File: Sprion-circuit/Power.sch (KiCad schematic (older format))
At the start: 27 parts, among them IC1 R3111N211A, IC2 TAR5SB50, J1 Conn_01x02_Female, Q1 Q_PMOS_GSD, Q2 Q_PMOS_GSD, SW1 SW_SPDT, U4 LXDC55FAAA-203

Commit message: Push, Push, Push
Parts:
- removed Q2: Q_PMOS_GSD, symbol Device:Q_PMOS_GSD
- added Q2: Q_NMOS_GSD, symbol Device:Q_NMOS_GSD
- C11: value C -> 0.1u
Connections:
- net +BATT: now also Q2.2 (S)
- net at C8.1, Q1.3 (D), R11.2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: now also Q2.3 (D)
- net at IC1.1 (OUT), R11.1: now also Q2.1 (G)
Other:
- moved on the sheet: C10, C11, C12, C13, C7, C8, C9, D1, IC1, IC2, J1, L1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

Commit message: :fix　いろいろ
後で書きます
とりあえず寝ます
許してください
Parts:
- added R32: 2.7, symbol Device:R
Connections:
- net +3.3VA: now also D1.2 (A)
- net +3V3: now also R32.2; no longer D1.2 (A), L1.1
- new net: L1.1, R32.1
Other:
- moved on the sheet: C12, C13, D1, L1, R12, R13, R14, R15, R16, R17, U4

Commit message: add,feat,fix:すまんコミットわすれててぐちゃぐちゃや
配置始めた。
フットプリント割り当てた
回路図pdfで吐いた
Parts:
- removed J1: Conn_01x02_Female, symbol Connector:Conn_01x02_Female
- removed U4: LXDC55FAAA-203, LXDC55FAAA203, symbol Sprion-circuit:LXDC55FAAA-203
- added C15: 0.1u, Capacitor_SMD:C_0603_1608Metric, symbol Device:C
- added J1: Conn_01x03_Female, Connector_JST:JST_PH_B3B-PH-K_1x03_P2.00mm_Vertical, symbol Connector:Conn_01x03_Female
- added R24, R25: 10k, Resistor_SMD:R_0603_1608Metric, symbol Device:R
- added U9: LXDC55FAAA-203, Sprion-circuit:LXDC55FAAA203, symbol Sprion-circuit:LXDC55FAAA-203
- C10, C11, C12, C13, C8, C9: footprint (none) -> Capacitor_SMD:C_0603_1608Metric
- C7: value CP -> 100u; footprint (none) -> Sprion-circuit:CAPPRD250W50D630H600
- D1: footprint (none) -> LED_SMD:LED_0603_1608Metric
- IC1, IC2: footprint (none) -> Package_TO_SOT_SMD:SOT-23-5
- L1: footprint (none) -> Inductor_SMD:L_1210_3225Metric
- Q1: value Q_PMOS_GSD -> IRML6402; footprint (none) -> Package_TO_SOT_SMD:SOT-23
- Q2: value Q_NMOS_GSD -> IRFML8244; footprint (none) -> Package_TO_SOT_SMD:SOT-23
- R10, R11, R12, R13, R14, R15, R16, R32, R7, R8, R9: footprint (none) -> Resistor_SMD:R_0603_1608Metric
- R17: value R -> 330; footprint (none) -> Resistor_SMD:R_0603_1608Metric
- SW1: value SW_SPDT -> SSAJ120100; footprint (none) -> Sprion-circuit:s
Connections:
- net +3.3VA: now also R24.1; no longer D1.2 (A)
- net +3V3: now also D1.2 (A), U9.7 (VOUT_1), U9.8 (VOUT_2), U9.9 (VOUT_3)
- net +BATT: now also U9.1 (EN), U9.3 (VIN_1)
- net GND: now also C15.2, J1.1 (Pin_1), R25.2, U9.12 (GND_2), U9.13 (GND_3), U9.14 (GND_4), U9.6 (GND_1)
- net at R12.2: now also U9.11 (FB)
- net at C7.1, Q1.2 (S), R7.2: now also J1.3 (Pin_3)
- new net: U9.4 (VIN_2), U9.5 (VIN_3)
- new net VREF: C15.1, R24.2, R25.1
- no-connect marks 1 -> 2

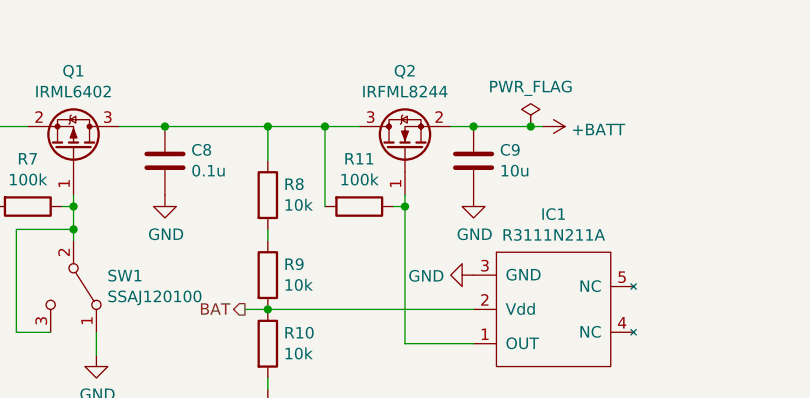
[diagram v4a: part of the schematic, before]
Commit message: fix: eschemaの微修正
ハイサイドスイッチをNch→Pchへ修正
bootをプルダウンに
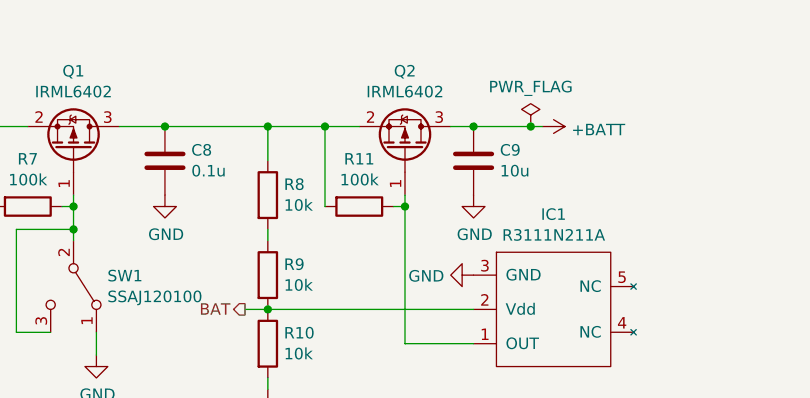
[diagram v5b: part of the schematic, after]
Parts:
- removed Q2: IRFML8244, Package_TO_SOT_SMD:SOT-23, symbol Device:Q_NMOS_GSD
- added Q2: IRML6402, Package_TO_SOT_SMD:SOT-23, symbol Device:Q_PMOS_GSD
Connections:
- net +BATT: now also Q2.3 (D)
- net at IC1.1 (OUT), R11.1: now also Q2.1 (G)
- net at C8.1, Q1.3 (D), R11.2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: now also Q2.2 (S)
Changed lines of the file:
@@
-$EndComp
-$Comp
-L Device:Q_NMOS_GSD Q2
-U 1 1 60E96580
-P 3950 2200
-F 0 "Q2" V 4292 2200 50  0000 C CNN
-F 1 "IRFML8244" V 4201 2200 50  0000 C CNN
-F 2 "Package_TO_SOT_SMD:SOT-23" H 4150 2300 50  0001 C CNN
-F 3 "~" H 3950 2200 50  0001 C CNN
-	1    3950 2200
-	0    -1   -1   0
 $EndComp
 $Comp
@@
 	0    -1   -1   0
 $EndComp
+$Comp
+L Device:Q_PMOS_GSD Q2
+U 1 1 61B67607
+P 3950 2200
+F 0 "Q2" V 4292 2200 50  0000 C CNN
+F 1 "IRML6402" V 4201 2200 50  0000 C CNN
+F 2 "Package_TO_SOT_SMD:SOT-23" H 4150 2300 50  0001 C CNN
+F 3 "~" H 3950 2200 50  0001 C CNN
+	1    3950 2200
+	0    1    -1   0
+$EndComp
 $EndSCHEMATC

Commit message: add fix feat: でけたー（コミットしてなくてごめん）
ベタ塗、配線、再配置等
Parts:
- removed Q2: IRML6402, Package_TO_SOT_SMD:SOT-23, symbol Device:Q_PMOS_GSD
- added Q2: IRFML8244, Package_TO_SOT_SMD:SOT-23, symbol Device:Q_NMOS_GSD
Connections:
- net +BATT: now also C8.1, Q1.3 (D), R8.1
- net GND: now also Q2.3 (D); no longer C7.2, C8.2, IC1.3 (GND), J1.1 (Pin_1), R10.2, SW1.1 (A)
- net at R11.1: now also C7.2, C8.2, IC1.3 (GND), J1.1 (Pin_1), R10.2, SW1.1 (A), Q2.2 (S); no longer IC1.1 (OUT)
- new net: IC1.1 (OUT), Q2.1 (G), R11.2
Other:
- moved on the sheet: C9, R11
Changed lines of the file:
@@
 $Descr A4 11693 8268
 encoding utf-8
-Sheet 2 6
+Sheet 6 6
 Title ""
 Date ""
@@
 $EndDescr
 $Comp
-L power:GND #PWR01
-U 1 1 60F3968F
-P 1400 2300
-F 0 "#PWR01" H 1400 2050 50  0001 C CNN
-F 1 "GND" V 1405 2172 50  0000 R CNN
-F 2 "" H 1400 2300 50  0001 C CNN
-F 3 "" H 1400 2300 50  0001 C CNN
-	1    1400 2300
-	0    -1   -1   0
-$EndComp
-$Comp
 L power:PWR_FLAG #FLG01
 U 1 1 60F3A851
-P 1350 2300
-F 0 "#FLG01" H 1350 2375 50  0001 C CNN
-F 1 "PWR_FLAG" H 1350 2473 50  0000 C CNN
-F 2 "" H 1350 2300 50  0001 C CNN
-F 3 "~" H 1350 2300 50  0001 C CNN
-	1    1350 2300
-	-1   0    0    1
-$EndComp
-Wire Wire Line
-	1300 2300 1350 2300
-Wire Wire Line
-	1350 2300 1400 2300
-Connection ~ 1350 2300
+P 1700 4650
+F 0 "#FLG01" H 1700 4725 50  0001 C CNN
+F 1 "PWR_FLAG" H 1700 4823 50  0000 C CNN
+F 2 "" H 1700 4650 50  0001 C CNN
+F 3 "~" H 1700 4650 50  0001 C CNN
+	1    1700 4650
+	0    -1   -1   0
+$EndComp
 $Comp
 L Switch:SW_SPDT SW1
@@
 $EndComp
 $Comp
-L power:GND #PWR03
-U 1 1 60F431E5
-P 2600 3100
-F 0 "#PWR03" H 2600 2850 50  0001 C CNN
-F 1 "GND" H 2605 2927 50  0000 C CNN
-F 2 "" H 2600 3100 50  0001 C CNN
-F 3 "" H 2600 3100 50  0001 C CNN
-	1    2600 3100
-	1    0    0    -1
-$EndComp
-$Comp
 L Device:R R7
 U 1 1 60F43B12
@@
 L power:+BATT #PWR08
 U 1 1 60F46202
-P 4550 2100
-F 0 "#PWR08" H 4550 1950 50  0001 C CNN
-F 1 "+BATT" V 4565 2228 50  0000 L CNN
-F 2 "" H 4550 2100 50  0001 C CNN
-F 3 "" H 4550 2100 50  0001 C CNN
-	1    4550 2100
+P 3950 2100
+F 0 "#PWR08" H 3950 1950 50  0001 C CNN
+F 1 "+BATT" V 3965 2228 50  0000 L CNN
+F 2 "" H 3950 2100 50  0001 C CNN
+F 3 "" H 3950 2100 50  0001 C CNN
+	1    3950 2100
 	0    1    1    0
 $EndComp
@@
 L power:PWR_FLAG #FLG02
 U 1 1 60F505D9
-P 4500 2100
-F 0 "#FLG02" H 4500 2175 50  0001 C CNN
-F 1 "PWR_FLAG" H 4500 2273 50  0000 C CNN
-F 2 "" H 4500 2100 50  0001 C CNN
-F 3 "~" H 4500 2100 50  0001 C CNN
-	1    4500 2100
-	1    0    0    -1
-$EndComp
-$Comp
-L power:GND #PWR07
-U 1 1 60F5182C
-P 4250 2750
-F 0 "#PWR07" H 4250 2500 50  0001 C CNN
-F 1 "GND" V 4255 2622 50  0000 R CNN
-F 2 "" H 4250 2750 50  0001 C CNN
-F 3 "" H 4250 2750 50  0001 C CNN
-	1    4250 2750
-	0    1    1    0
-$EndComp
-Wire Wire Line
-	4550 2100 4500 2100
-Connection ~ 4500 2100
-$Comp
-L power:GND #PWR04
-U 1 1 60F5CE78
-P 2900 2400
-F 0 "#PWR04" H 2900 2150 50  0001 C CNN
-F 1 "GND" H 2905 2227 50  0000 C CNN
-F 2 "" H 2900 2400 50  0001 C CNN
-F 3 "" H 2900 2400 50  0001 C CNN
-	1    2900 2400
-	1    0    0    -1
-$EndComp
+P 3900 2100
+F 0 "#FLG02" H 3900 2175 50  0001 C CNN
+F 1 "PWR_FLAG" H 3900 2273 50  0000 C CNN
+F 2 "" H 3900 2100 50  0001 C CNN
+F 3 "~" H 3900 2100 50  0001 C CNN
+	1    3900 2100
+	1    0    0    -1
+$EndComp
+Wire Wire Line
+	3950 2100 3900 2100
+Connection ~ 3900 2100
 $Comp
 L Device:C C8
@@
 	1    0    0    -1
 $EndComp
-$Comp
-L power:GND #PWR05
-U 1 1 60F66160
-P 3350 3250
-F 0 "#PWR05" H 3350 3000 50  0001 C CNN
-F 1 "GND" H 3355 3077 50  0000 C CNN
-F 2 "" H 3350 3250 50  0001 C CNN
-F 3 "" H 3350 3250 50  0001 C CNN
-	1    3350 3250
-	1    0    0    -1
-$EndComp
-Wire Wire Line
-	3350 3200 3350 3250
 Wire Wire Line
 	2700 2100 2900 2100
 Wire Wire Line
-	3950 2400 3950 2450
-Wire Wire Line
-	3950 3050 4250 3050
-$Comp
-L Device:R R11
-U 1 1 60F7E679
-P 3750 2450
-F 0 "R11" V 3543 2450 50  0000 C CNN
-F 1 "100k" V 3634 2450 50  0000 C CNN
-F 2 "Resistor_SMD:R_0603_1608Metric" V 3680 2450 50  0001 C CNN
-F 3 "~" H 3750 2450 50  0001 C CNN
-	1    3750 2450
-	0    1    1    0
-$EndComp
-Wire Wire Line
-	3900 2450 3950 2450
-Connection ~ 3950 2450
-Wire Wire Line
-	3600 2450 3600 2100
-Connection ~ 3600 2100
-Wire Wire Line
-	3600 2100 3750 2100
-Wire Wire Line
 	3350 2900 4250 2900
-Wire Wire Line
-	3950 2450 3950 3050
 Connection ~ 2900 2100
 Wire Wire Line
@@
 	1850 2100 2150 2100
 Connection ~ 2150 2100
-$Comp
-L power:GND #PWR02
-U 1 1 60F8B6AE
-P 1850 2450
-F 0 "#PWR02" H 1850 2200 50  0001 C CNN
-F 1 "GND" H 1855 2277 50  0000 C CNN
-F 2 "" H 1850 2450 50  0001 C CNN
-F 3 "" H 1850 2450 50  0001 C CNN
-	1    1850 2450
-	1    0    0    -1
-$EndComp
 Wire Wire Line
 	1850 2400 1850 2450
@@
 L Device:C C9
 U 1 1 60F9001F
-P 4250 2250
-F 0 "C9" H 4365 2296 50  0000 L CNN
-F 1 "10u" H 4365 2205 50  0000 L CNN
-F 2 "Capacitor_SMD:C_0603_1608Metric" H 4288 2100 50  0001 C CNN
-F 3 "~" H 4250 2250 50  0001 C CNN
-	1    4250 2250
+P 3650 2250
+F 0 "C9" H 3765 2296 50  0000 L CNN
+F 1 "10u" H 3765 2205 50  0000 L CNN
+F 2 "Capacitor_SMD:C_0603_1608Metric" H 3688 2100 50  0001 C CNN
+F 3 "~" H 3650 2250 50  0001 C CNN
+	1    3650 2250
 	1    0    0    -1
 $EndComp
@@
 L power:GND #PWR06
 U 1 1 60F90B97
-P 4250 2400
-F 0 "#PWR06" H 4250 2150 50  0001 C CNN
-F 1 "GND" H 4255 2227 50  0000 C CNN
-F 2 "" H 4250 2400 50  0001 C CNN
-F 3 "" H 4250 2400 50  0001 C CNN
-	1    4250 2400
-	1    0    0    -1
-$EndComp
-Wire Wire Line
-	4150 2100 4250 2100
-Wire Wire Line
-	4250 2100 4500 2100
-Connection ~ 4250 2100
+P 3650 2400
+F 0 "#PWR06" H 3650 2150 50  0001 C CNN
+F 1 "GND" H 3655 2227 50  0000 C CNN
+F 2 "" H 3650 2400 50  0001 C CNN
+F 3 "" H 3650 2400 50  0001 C CNN
+	1    3650 2400
+	1    0    0    -1
+$EndComp
+Wire Wire Line
+	3650 2100 3900 2100
 $Comp
 L Device:R R8
@@
 Wire Wire Line
 	2900 2100 3350 2100
-Connection ~ 3350 2100
-Wire Wire Line
-	3350 2100 3600 2100
 Wire Wire Line
 	3350 2550 3350 2600
@@
 	0    -1   -1   0
 $EndComp
-$Comp
-L Device:Q_PMOS_GSD Q2
-U 1 1 61B67607
-P 3950 2200
-F 0 "Q2" V 4292 2200 50  0000 C CNN
-F 1 "IRML6402" V 4201 2200 50  0000 C CNN
-F 2 "Package_TO_SOT_SMD:SOT-23" H 4150 2300 50  0001 C CNN
-F 3 "~" H 3950 2200 50  0001 C CNN
-	1    3950 2200
-	0    1    -1   0
-$EndComp
+Wire Wire Line
+	3350 2100 3650 2100
+Connection ~ 3350 2100
+Connection ~ 3650 2100
+$Comp
+L Device:R R11
+U 1 1 60F7E679
+P 2050 3900
+F 0 "R11" V 1843 3900 50  0000 C CNN
+F 1 "100k" V 1934 3900 50  0000 C CNN
+F 2 "Resistor_SMD:R_0603_1608Metric" V 1980 3900 50  0001 C CNN
+F 3 "~" H 2050 3900 50  0001 C CNN
+	1    2050 3900
+	1    0    0    -1
+$EndComp
+$Comp
+L Device:Q_NMOS_GSD Q2
+U 1 1 61B98387
+P 1800 4050
+F 0 "Q2" H 2005 4096 50  0000 L CNN
+F 1 "IRFML8244" H 2005 4005 50  0000 L CNN
+F 2 "Package_TO_SOT_SMD:SOT-23" H 2000 4150 50  0001 C CNN
+F 3 "~" H 1800 4050 50  0001 C CNN
+	1    1800 4050
+	-1   0    0    1
+$EndComp
+Connection ~ 1700 4650
+Wire Wire Line
+	1700 4650 1700 4700
+$Comp
+L power:GND #PWR01
+U 1 1 60F3968F
+P 1700 4700
+F 0 "#PWR01" H 1700 4450 50  0001 C CNN
+F 1 "GND" V 1705 4572 50  0000 R CNN
+F 2 "" H 1700 4700 50  0001 C CNN
+F 3 "" H 1700 4700 50  0001 C CNN
+	1    1700 4700
+	1    0    0    -1
+$EndComp
+Wire Wire Line
+	1700 4250 1700 4650
+Wire Wire Line
+	2000 4050 2050 4050
+Connection ~ 2050 4050
+Wire Wire Line
+	2050 4050 4250 4050
+Wire Wire Line
+	1700 3850 1700 3700
+Wire Wire Line
+	1700 2300 1450 2300
+Wire Wire Line
+	1700 3700 2050 3700
+Wire Wire Line
+	2050 3700 2050 3750
+Connection ~ 1700 3700
+Wire Wire Line
+	1700 2300 1700 2450
+Wire Wire Line
+	4250 3050 4250 4050
+Wire Wire Line
+	3350 3450 1700 3450
+Wire Wire Line
+	3350 3200 3350 3450
+Connection ~ 1700 3450
+Wire Wire Line
+	1700 3450 1700 3600
+Wire Wire Line
+	2600 3100 1700 3100
+Connection ~ 1700 3100
+Wire Wire Line
+	1700 3100 1700 3250
+Wire Wire Line
+	1850 2450 1700 2450
+Connection ~ 1700 2450
+Wire Wire Line
+	1700 2450 1700 3100
+Wire Wire Line
+	2900 2400 2900 3250
+Wire Wire Line
+	2900 3250 1700 3250
+Connection ~ 1700 3250
+Wire Wire Line
+	1700 3250 1700 3450
+Wire Wire Line
+	4250 2750 3800 2750
+Wire Wire Line
+	3800 2750 3800 3600
+Wire Wire Line
+	3800 3600 1700 3600
+Connection ~ 1700 3600
+Wire Wire Line
+	1700 3600 1700 3700
+$Comp
+L power:PWR_FLAG #FLG0101
+U 1 1 61C050C7
+P 1450 2300
+F 0 "#FLG0101" H 1450 2375 50  0001 C CNN
+F 1 "PWR_FLAG" H 1450 2473 50  0000 C CNN
+F 2 "" H 1450 2300 50  0001 C CNN
+F 3 "~" H 1450 2300 50  0001 C CNN
+	1    1450 2300
+	-1   0    0    1
+$EndComp
+Connection ~ 1450 2300
+Wire Wire Line
+	1450 2300 1300 2300
 $EndSCHEMATC
